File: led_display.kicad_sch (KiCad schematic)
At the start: 164 parts, among them J1 Conn_01x02_Female, J2 Conn_01x08_Male, J3 Conn_01x08_Male, J4 Conn_02x05_Odd_Even, Q1 Q_PMOS_GSD, Q10 Q_PMOS_GSD, Q11 Q_NMOS_GSD, Q12 Q_NMOS_GSD, Q13 Q_NMOS_GSD, Q14 Q_NMOS_GSD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

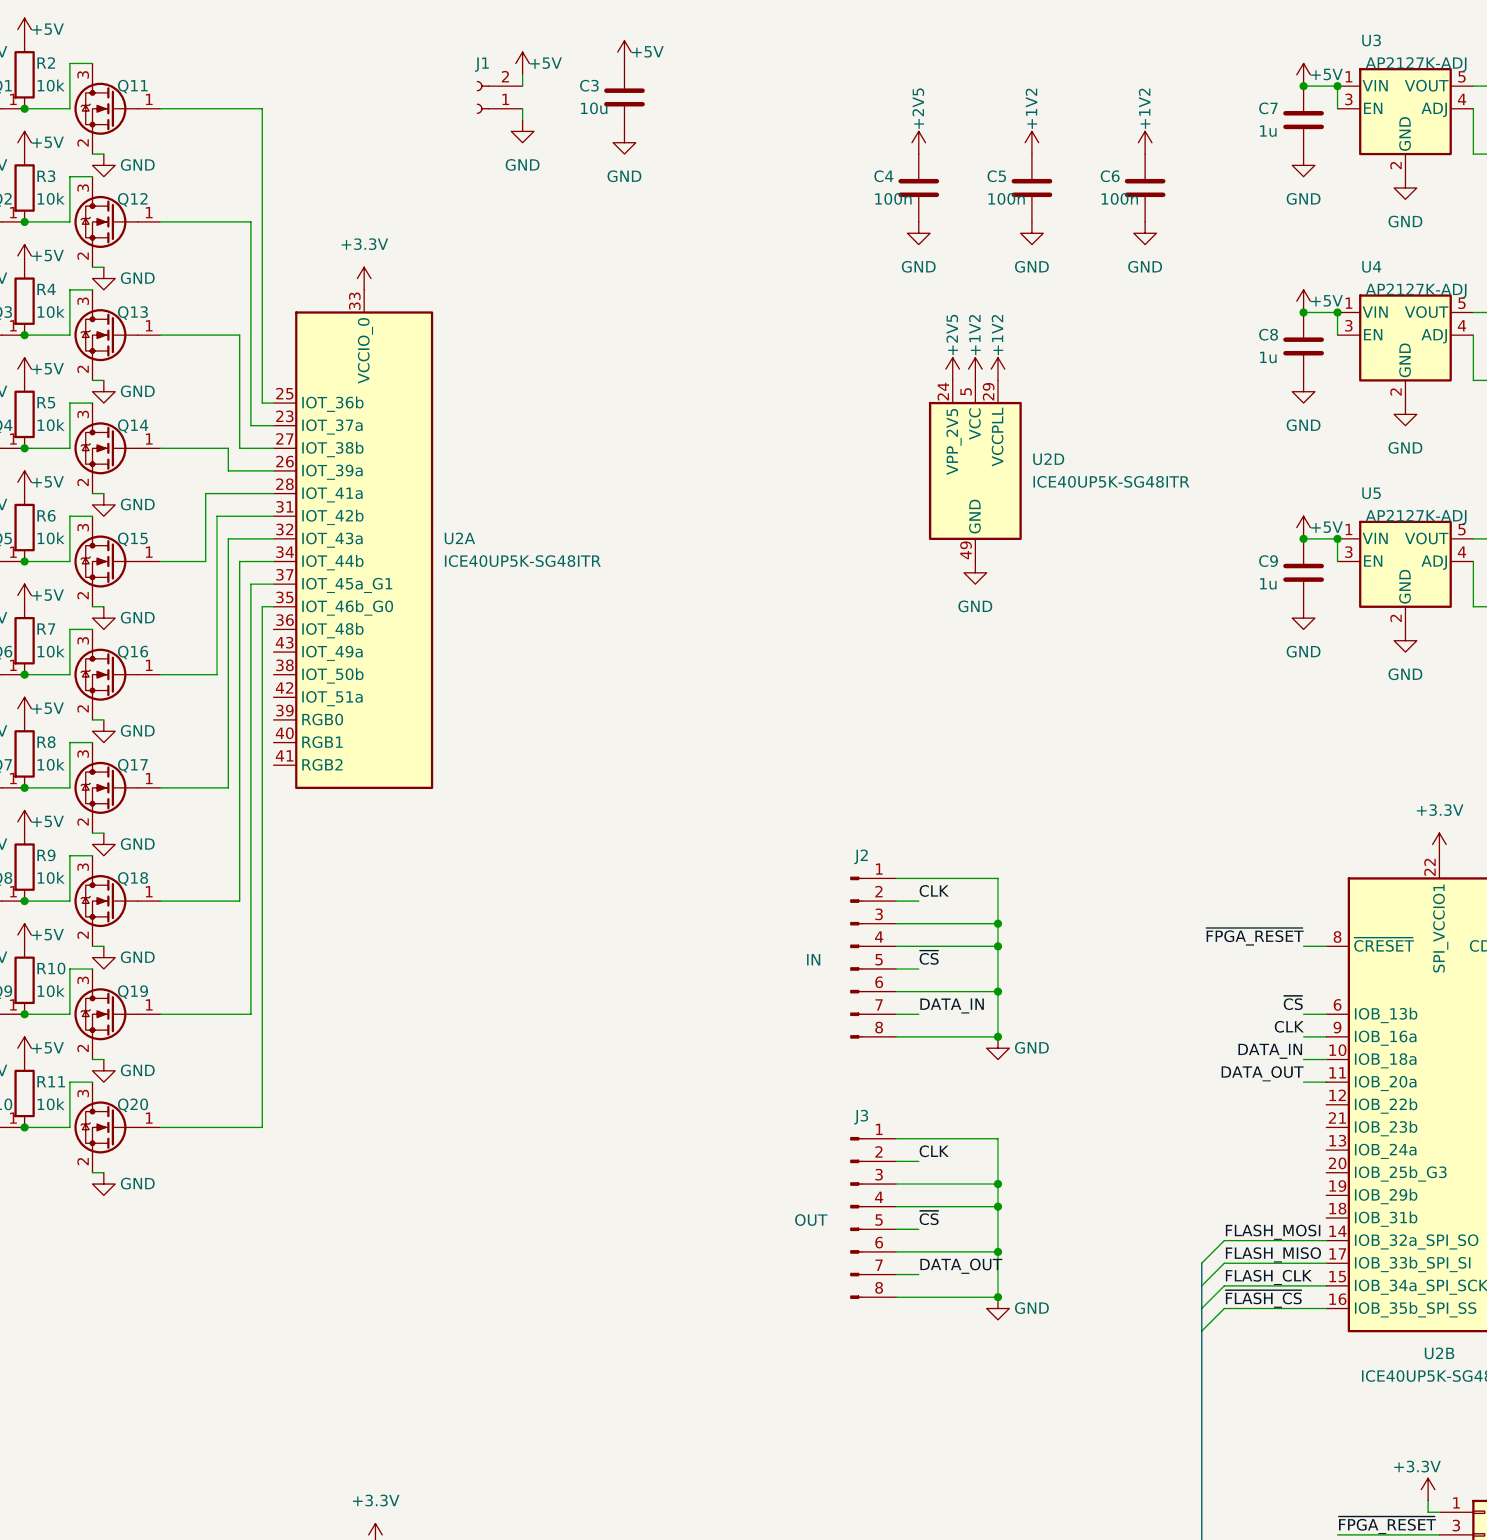
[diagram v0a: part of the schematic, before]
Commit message: added FPGA
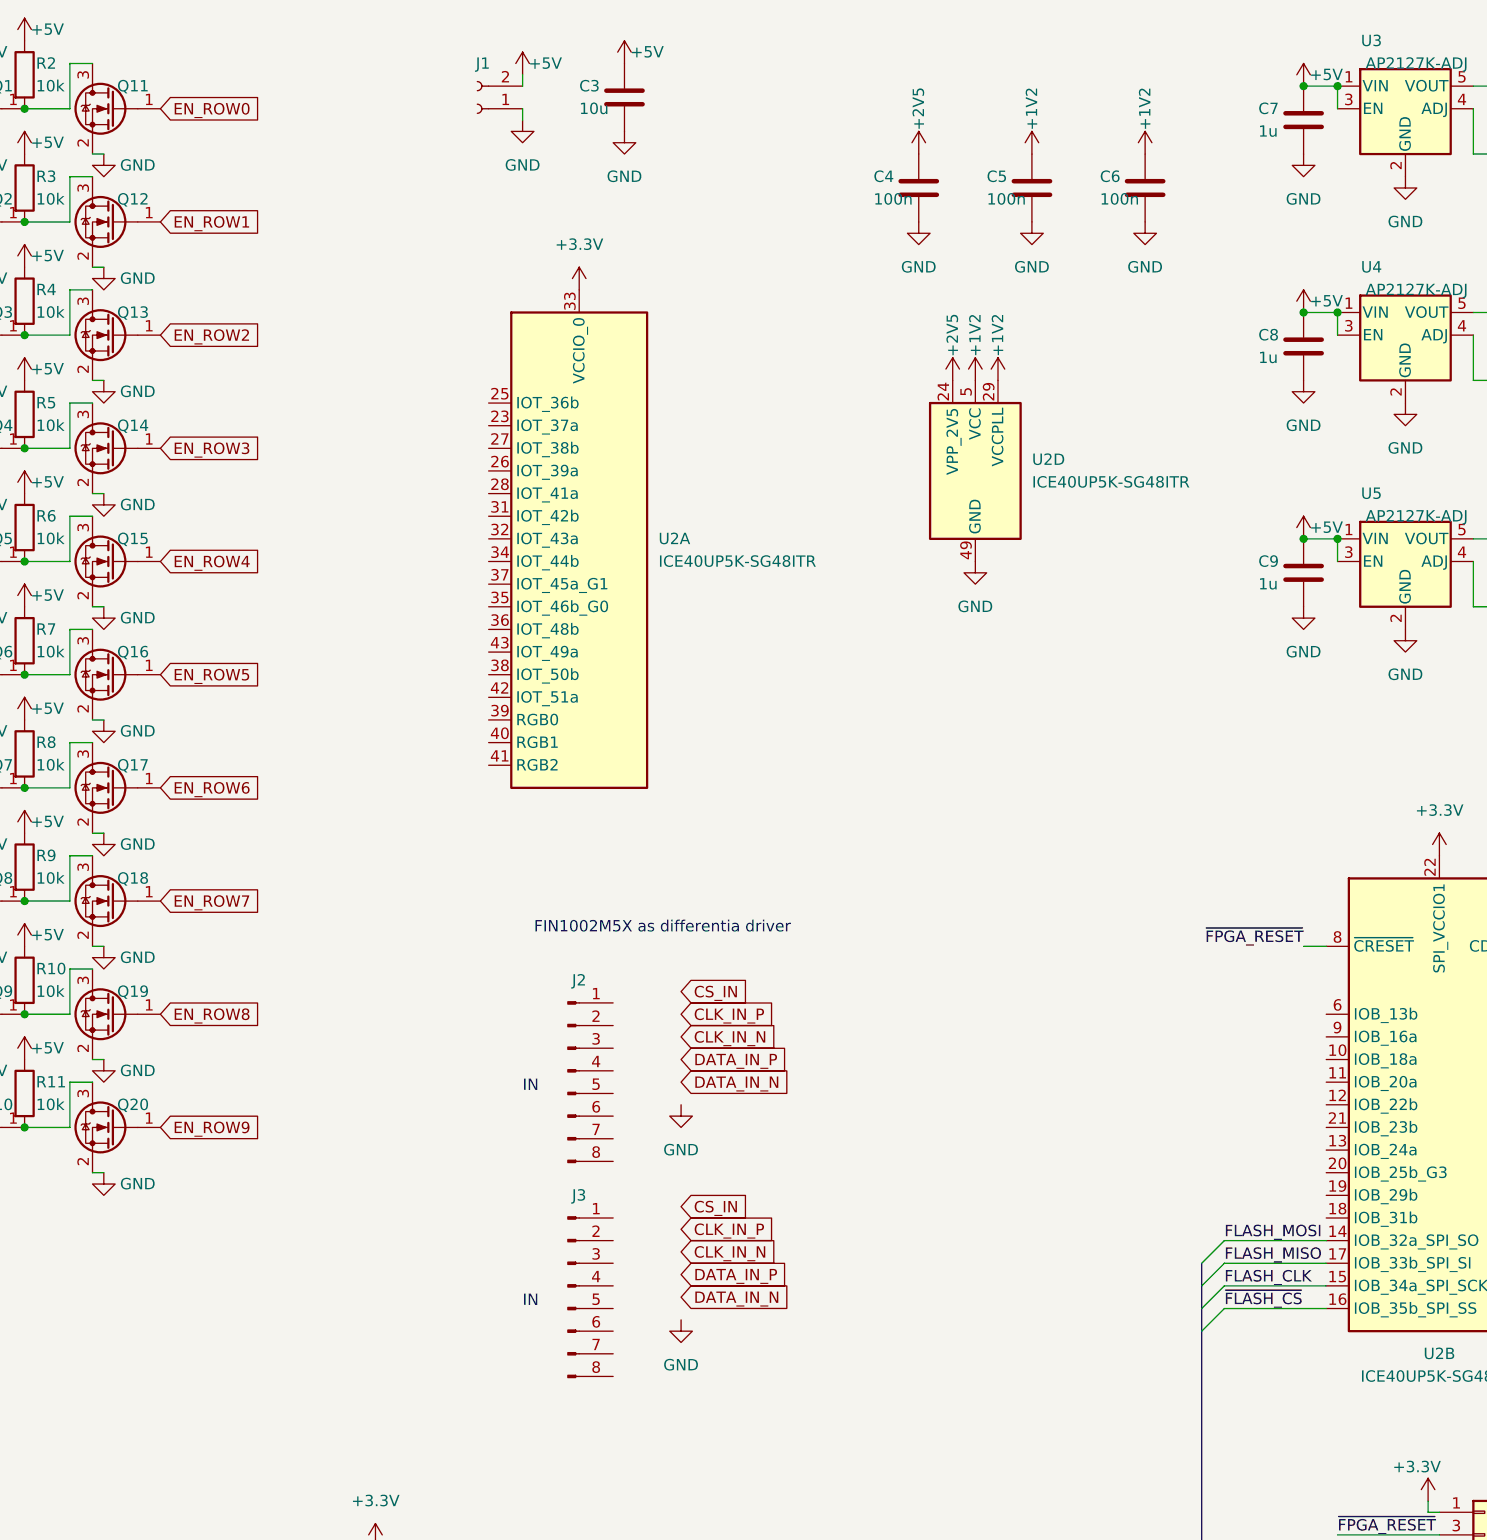
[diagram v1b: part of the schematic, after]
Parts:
- J1: footprint Connector_AMASS:AMASS_XT30PW-M_1x02_P2.50mm_Horizontal -> Connector_Molex:Molex_PicoBlade_53261-0271_1x02-1MP_P1.25mm_Horizontal
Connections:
- net GND: no longer J2.1 (Pin_1), J2.3 (Pin_3), J2.4 (Pin_4), J2.6 (Pin_6), J2.8 (Pin_8), J3.1 (Pin_1), J3.3 (Pin_3), J3.4 (Pin_4), J3.6 (Pin_6), J3.8 (Pin_8)
- net at U2.23 (IOT_37a): no longer Q12.1 (G)
- net at U2.25 (IOT_36b): no longer Q11.1 (G)
- net at U2.26 (IOT_39a): no longer Q14.1 (G)
- net at U2.27 (IOT_38b): no longer Q13.1 (G)
- net at U2.28 (IOT_41a): no longer Q15.1 (G)
- net at U2.31 (IOT_42b): no longer Q16.1 (G)
- net at U2.32 (IOT_43a): no longer Q17.1 (G)
- net at U2.34 (IOT_44b): no longer Q18.1 (G)
- net at U2.35 (IOT_46b_G0): no longer Q20.1 (G)
- net at U2.37 (IOT_45a_G1): no longer Q19.1 (G)
- removed net CLK: J2.2 (Pin_2), J3.2 (Pin_2), U2.9 (IOB_16a)
- net DATA_IN: no longer names the net of U2.10 (IOB_18a)
- net DATA_IN: no longer J2.7 (Pin_7)
- net DATA_OUT: no longer names the net of U2.11 (IOB_20a)
- net DATA_OUT: no longer J3.7 (Pin_7)
- removed net ~{CS}: J2.5 (Pin_5), J3.5 (Pin_5), U2.6 (IOB_13b)
- new net EN_ROW0: Q11.1 (G)
- new net EN_ROW1: Q12.1 (G)
- new net EN_ROW2: Q13.1 (G)
- new net EN_ROW3: Q14.1 (G)
- new net EN_ROW4: Q15.1 (G)
- new net EN_ROW5: Q16.1 (G)
- new net EN_ROW6: Q17.1 (G)
- new net EN_ROW7: Q18.1 (G)
- new net EN_ROW8: Q19.1 (G)
- new net EN_ROW9: Q20.1 (G)
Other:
- note added: "FIN1002M5X as differentia driver"
- note removed: "OUT"
- moved on the sheet: J2, U2A

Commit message: layout of supply
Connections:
- net DRIVER_EN: now also U2.34 (IOT_44b); no longer U2.48 (IOB_4a)
- net DRIVER_SCL: now also R12.2, U2.35 (IOT_46b_G0); no longer R13.2, U2.47 (IOB_2a)
- net DRIVER_SDA: now also R13.2, U2.36 (IOT_48b); no longer R12.2, U2.44 (IOB_3b_G6)
- net EN_ROW_6: now reaches U2.31 (IOT_42b)
- net EN_ROW_7: now reaches U2.32 (IOT_43a)
- net EN_ROW_8: now reaches U2.37 (IOT_45a_G1)
- net EN_ROW_9: now reaches U2.38 (IOT_50b)
